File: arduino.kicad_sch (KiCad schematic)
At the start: 9 parts, among them J6 Conn_01x01_Female, J7 Conn_01x01_Female, U11 74HC4051, U4 LM358, U5 74HC4051

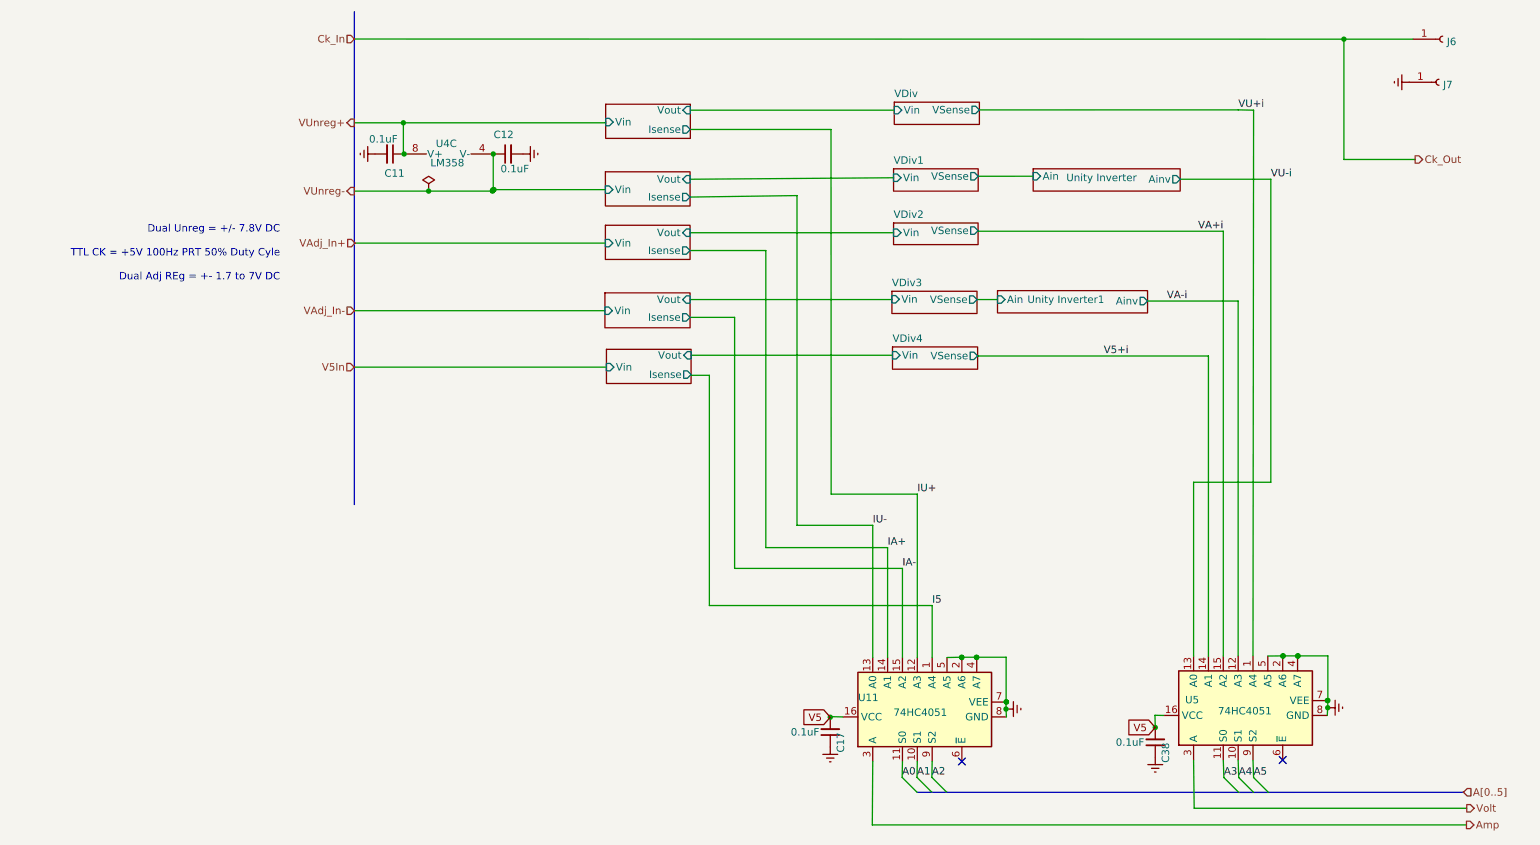
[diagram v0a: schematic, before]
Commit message: repositioned signal wires and started mapping OLED and rotary encoder
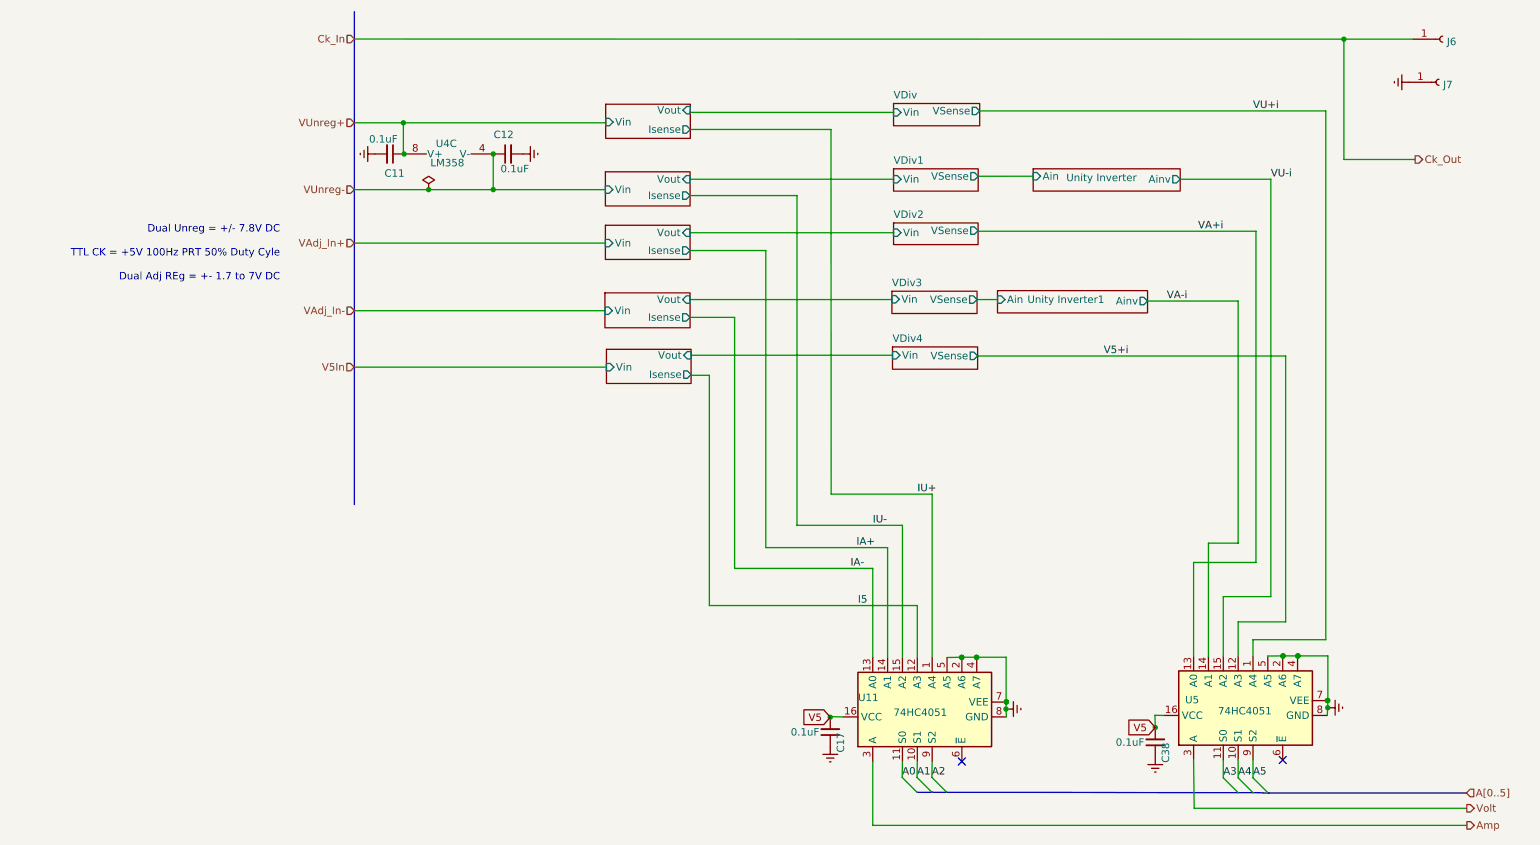
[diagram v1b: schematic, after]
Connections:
- net I5: now also U11.12 (A3); no longer U11.1 (A4)
- net IA-: now also U11.13 (A0); no longer U11.15 (A2)
- net IU+: now also U11.1 (A4); no longer U11.12 (A3)
- net IU-: now also U11.15 (A2); no longer U11.13 (A0)
- net V5+i: now also U5.12 (A3); no longer U5.14 (A1)
- net VA+i: now also U5.13 (A0); no longer U5.15 (A2)
- net VA-i: now also U5.14 (A1); no longer U5.12 (A3)
- net VU-i: now also U5.15 (A2); no longer U5.13 (A0)

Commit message: adding diff and summing amps to scale amp inputs
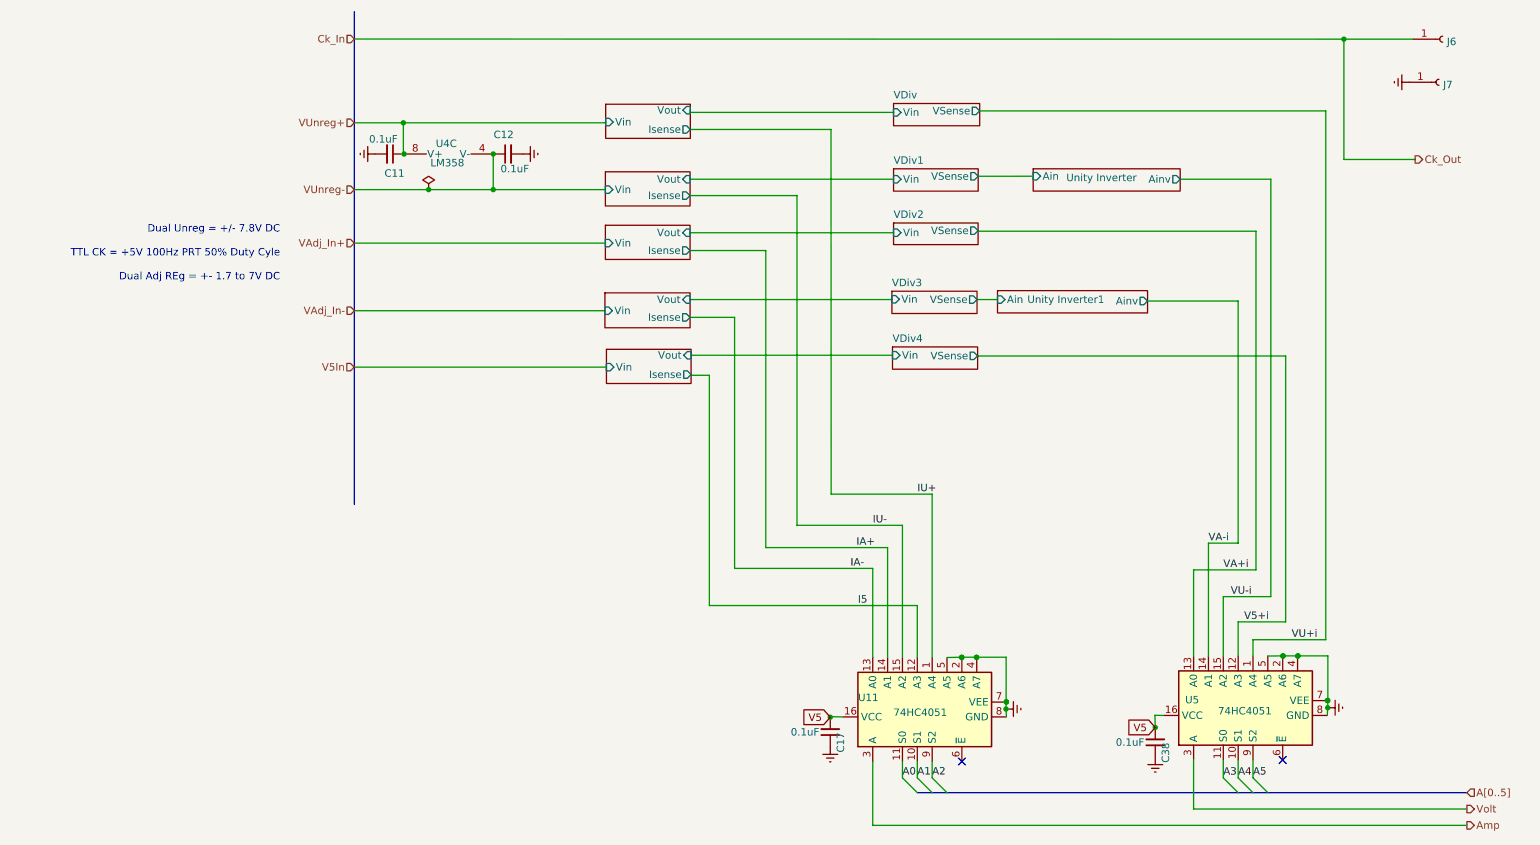
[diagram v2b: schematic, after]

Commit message: added new op amps and used automated traces due to complexity
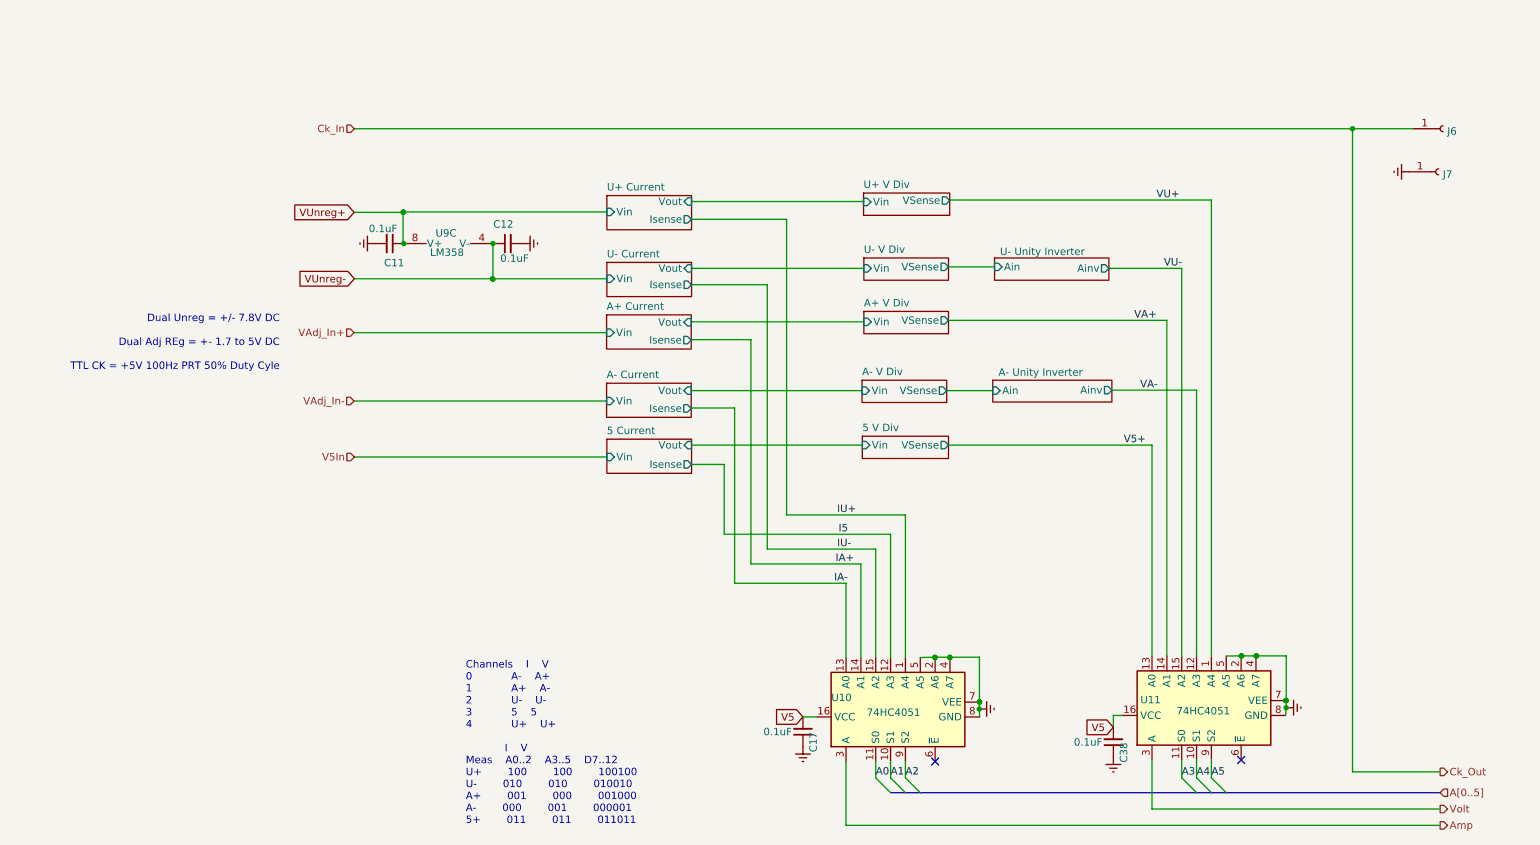
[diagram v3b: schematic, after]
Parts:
- U9: renamed from U4; footprint Package_TO_SOT_SMD:SOT-223-8 -> Package_SO:TSSOP-8_4.4x3mm_P0.65mm
- renumbered U11 to U10, U5 to U11
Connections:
- net V5+i renamed VA-
- net VA+i renamed V5+
- net VA-i renamed VA+
- net VU+i renamed VU+
- net VU-i renamed VU-
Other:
- sheet Curent and Volt4 renamed U+ Current
- sheet Curent and Volt5 renamed U- Current
- sheet Curent and Volt6 renamed A+ Current
- sheet Curent and Volt7 renamed A- Current
- sheet Curent and Volt8 renamed 5 Current
- sheet Unity Inverter renamed U- Unity Inverter
- sheet Unity Inverter1 renamed A- Unity Inverter
- sheet VDiv renamed U+ V Div
- sheet VDiv1 renamed U- V Div
- sheet VDiv2 renamed A+ V Div
- sheet VDiv3 renamed A- V Div
- sheet VDiv4 renamed 5 V Div
- note added: "Channels I V 0 A- A+ 1 A+ A- 2 U- U- 3 5 5 4 U+ U+ I V Meas A0..2 A3..5 D7..12 U+ 100 100 100100 U- 010 010 010010 A+ 001 000 001000 A- 000 001 000001 5+ 011 011 011011"
- note added: "Dual Unreg = +/- 7.8V DC Dual Adj REg = +- 1.7 to 5V DC TTL CK = +5V 100Hz PRT 50% Duty Cyle"
- note removed: "Dual Unreg = +/- 7.8V DC TTL CK = +5V 100Hz PRT 50% Duty Cyle Dual Adj REg = +- 1.7 to 7V DC"
- moved on the sheet: C11, C12, C17, C38, J6, J7, U10, U11, U9C

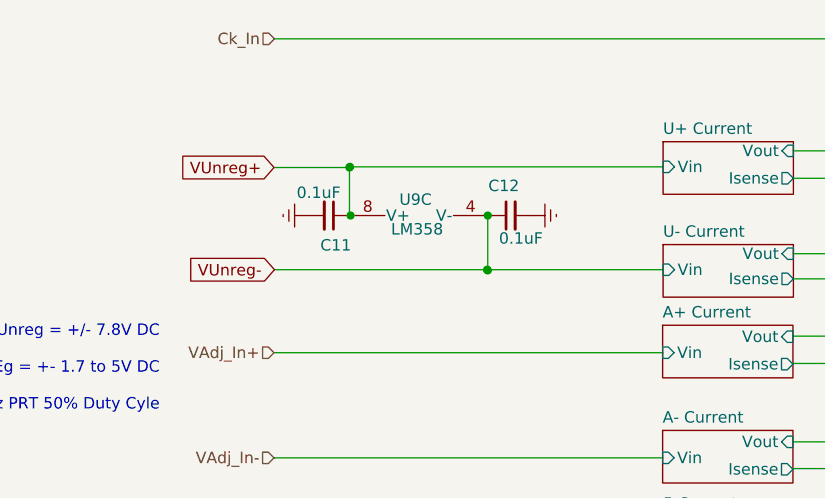
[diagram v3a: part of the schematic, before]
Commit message: new EMC-EMI layout with improved suppression
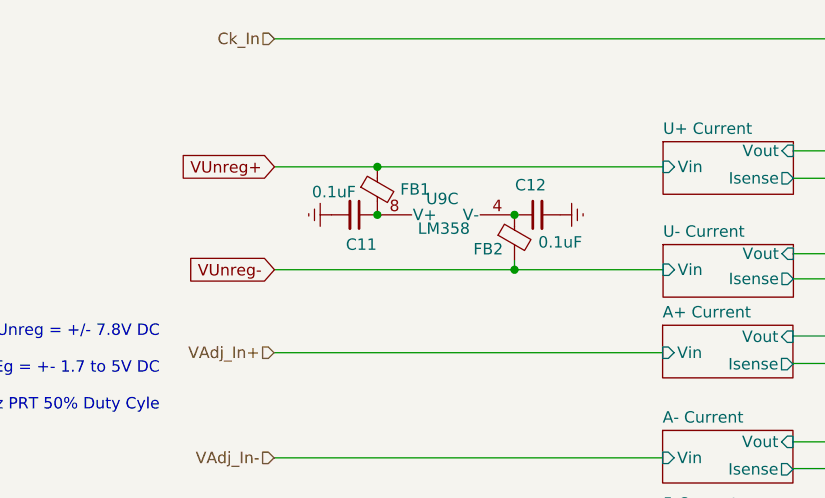
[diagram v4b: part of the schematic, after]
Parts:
- added FB1, FB2: FerriteBead_Small, Inductor_SMD:L_0603_1608Metric, symbol Device:FerriteBead_Small
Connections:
- net VUnreg+: now also FB1.1; no longer C11.1, U9.8 (V+)
- net VUnreg-: now also FB2.2; no longer C12.1, U9.4 (V-)
- new net: C11.1, FB1.2, U9.8 (V+)
- new net: C12.1, FB2.1, U9.4 (V-)
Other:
- moved on the sheet: C11, C12, U9C

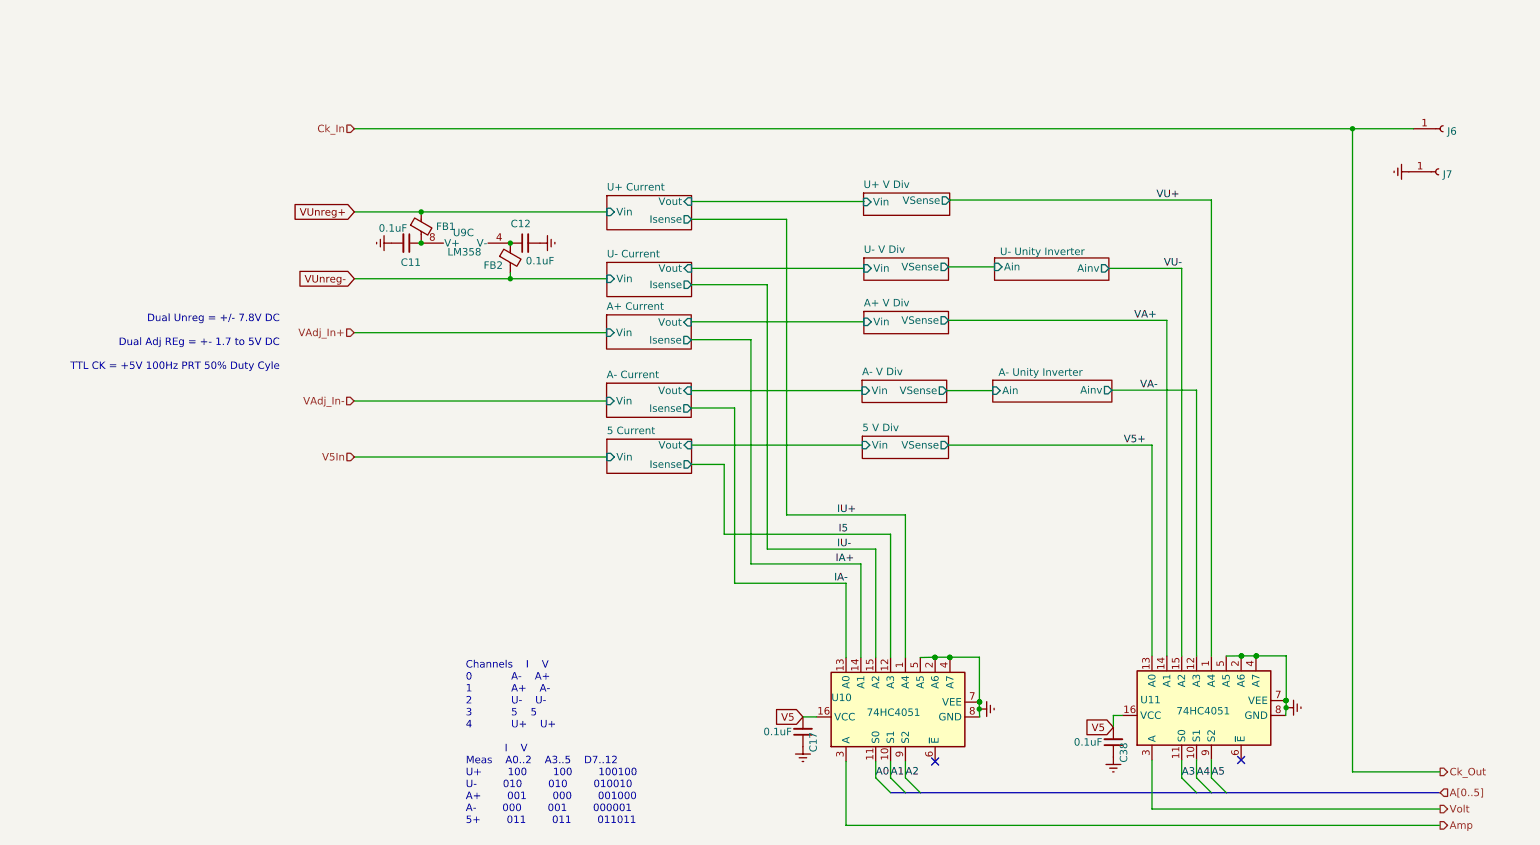
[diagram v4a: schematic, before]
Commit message: updates with foot print guard rings
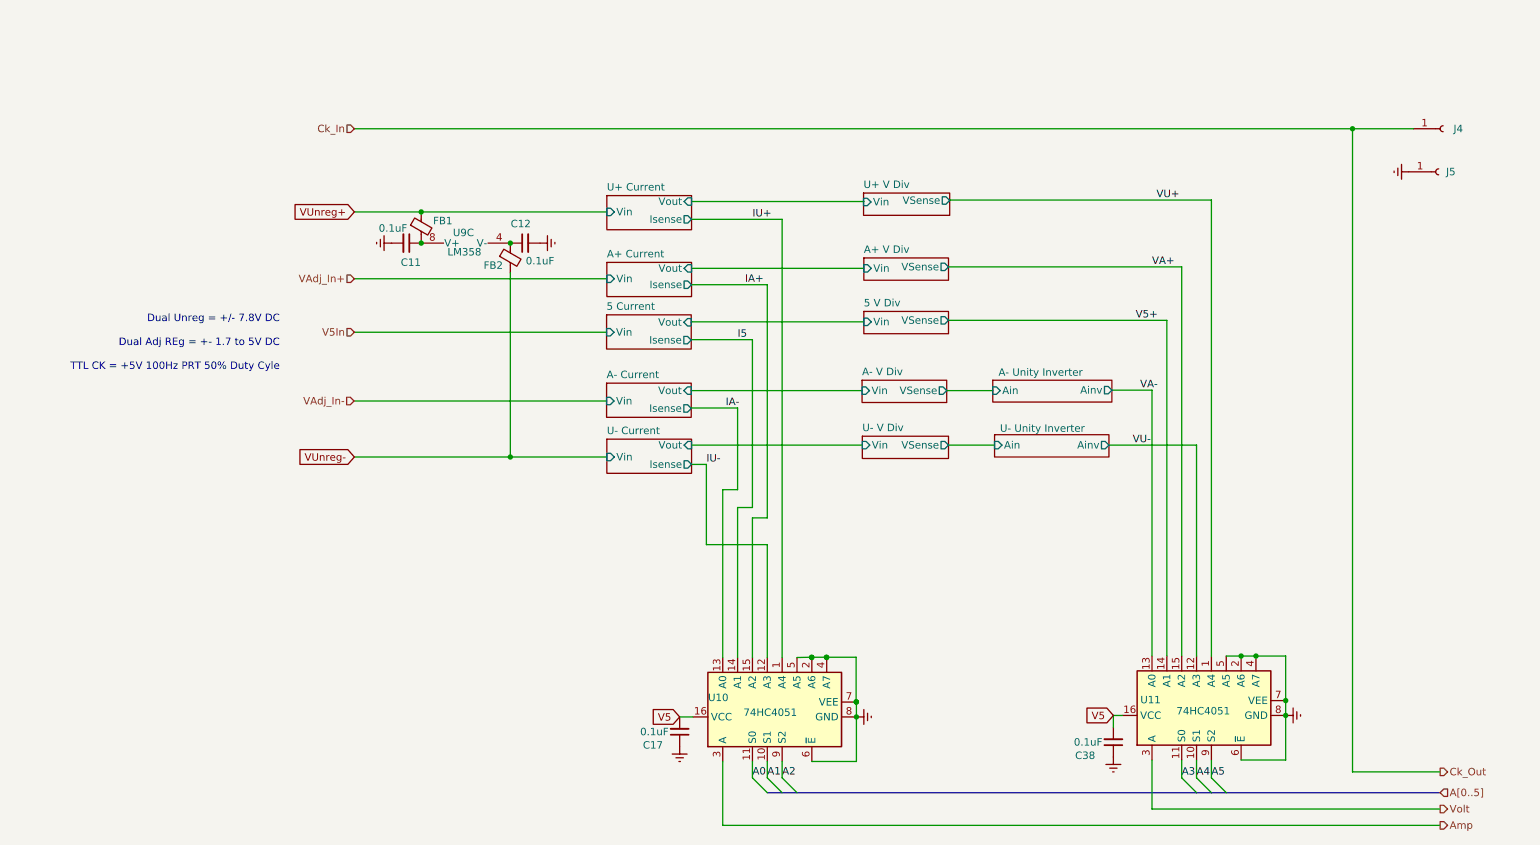
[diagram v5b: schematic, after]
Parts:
- renumbered J6 to J4, J7 to J5
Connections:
- net GNDREF: now also U10.6 (~{E}), U11.6 (~{E})
- net I5: now also U10.14 (A1); no longer U10.12 (A3)
- net IA+: now also U10.15 (A2); no longer U10.14 (A1)
- net IU-: now also U10.12 (A3); no longer U10.15 (A2)
- net V5+: now also U11.14 (A1); no longer U11.13 (A0)
- net VA+: now also U11.15 (A2); no longer U11.14 (A1)
- net VA-: now also U11.13 (A0); no longer U11.12 (A3)
- net VU-: now also U11.12 (A3); no longer U11.15 (A2)
- no-connect marks 2 -> 0
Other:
- note removed: "Channels I V 0 A- A+ 1 A+ A- 2 U- U- 3 5 5 4 U+ U+ I V Meas A0..2 A3..5 D7..12 U+ 100 100 100100 U- 010 010 010010 A+ 001 000 001000 A- 000 001 000001 5+ 011 011 011011"
- moved on the sheet: C17, U10

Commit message: working on MUX and pre-amp layout
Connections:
- net VUnreg-: now also FB2.1; no longer FB2.2
- net at C12.1, U9.4 (V-): now also FB2.2; no longer FB2.1
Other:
- moved on the sheet: C11, C12, FB1, FB2, U9C
